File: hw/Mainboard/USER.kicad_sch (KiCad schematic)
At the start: 4 parts, among them J13 USER, J14 USER_HEADER

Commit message: hw: 2x config switch (wip)
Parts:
- renumbered J13 to J12, J14 to J13
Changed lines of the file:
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@@
   (symbol (lib_id "Retrocomputing:CBM_PET_USER_Conn_02x12_Card_Edge") (at 106.68 93.98 0) (unit 1)
     (in_bom yes) (on_board yes)
-    (property "Reference" "J13" (id 0) (at 107.95 75.7682 0))
+    (property "Reference" "J12" (id 0) (at 107.95 75.7682 0))
     (property "Value" "USER" (id 1) (at 107.95 78.0796 0))
     (property "Footprint" "Retrocomputing:CBM_PET_USER_EDGE_CON_24P" (id 2) (at 106.68 93.98 0)
@@
   (symbol (lib_id "Connector_Generic:Conn_02x11_Odd_Even") (at 176.53 95.25 0) (mirror x) (unit 1)
     (in_bom yes) (on_board yes) (fields_autoplaced)
-    (property "Reference" "J14" (id 0) (at 177.8 76.2 0))
+    (property "Reference" "J13" (id 0) (at 177.8 76.2 0))
     (property "Value" "USER_HEADER" (id 1) (at 177.8 78.74 0))
     (property "Footprint" "Connector_PinHeader_2.54mm:PinHeader_2x11_P2.54mm_Vertical" (id 2) (at 176.53 95.25 0)
@@
   (symbol (lib_id "PET:PD_GND") (at 107.95 111.76 0) (unit 1)
     (in_bom yes) (on_board yes) (fields_autoplaced)
-    (property "Reference" "#PWR0107" (id 0) (at 107.95 118.11 0)
+    (property "Reference" "#PWR0113" (id 0) (at 107.95 118.11 0)
       (effects (font (size 1.27 1.27)) hide)
     )
@@
   (symbol (lib_id "PET:PD_GND") (at 133.35 82.55 0) (unit 1)
     (in_bom yes) (on_board yes) (fields_autoplaced)
-    (property "Reference" "#PWR0105" (id 0) (at 133.35 88.9 0)
+    (property "Reference" "#PWR0111" (id 0) (at 133.35 88.9 0)
       (effects (font (size 1.27 1.27)) hide)
     )
@@
   (symbol (lib_id "PET:PD_GND") (at 171.45 109.22 0) (unit 1)
     (in_bom yes) (on_board yes) (fields_autoplaced)
-    (property "Reference" "#PWR0106" (id 0) (at 171.45 115.57 0)
+    (property "Reference" "#PWR0112" (id 0) (at 171.45 115.57 0)
       (effects (font (size 1.27 1.27)) hide)
     )
@@
   (symbol (lib_id "power:+5V") (at 85.09 78.74 0) (mirror y) (unit 1)
     (in_bom yes) (on_board yes)
-    (property "Reference" "#PWR0104" (id 0) (at 85.09 82.55 0)
+    (property "Reference" "#PWR0110" (id 0) (at 85.09 82.55 0)
       (effects (font (size 1.27 1.27)) hide)
     )

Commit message: hw: header_and_jumper, button for flashing (wip)
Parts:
- JP1: footprint Jumper:SolderJumper-3_P1.3mm_Open_RoundedPad1.0x1.5mm -> PET:PinHeader_and_Jumper_1x03_P2.54mm_Vertical
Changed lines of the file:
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@@
     (property "Reference" "JP1" (id 0) (at 69.85 73.66 0))
     (property "Value" "VIDEO_OR_5V" (id 1) (at 69.85 76.2 0))
-    (property "Footprint" "Jumper:SolderJumper-3_P1.3mm_Open_RoundedPad1.0x1.5mm" (id 2) (at 69.85 78.74 0)
+    (property "Footprint" "PET:PinHeader_and_Jumper_1x03_P2.54mm_Vertical" (id 2) (at 69.85 78.74 0)
       (effects (font (size 1.27 1.27)) hide)
     )

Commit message: hw: caps & logos (wip)
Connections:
- net VCC is gone; now on net +5V: J13.2 (Pin_2), JP1.3 (B), PT37.2
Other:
- title: CBM PET Mainboard Replacement -> EconoPET 40/8096
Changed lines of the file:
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@@
   (paper "A")
   (title_block
-    (title "CBM PET Mainboard Replacement")
+    (title "EconoPET 40/8096")
+    (date "2023-10-01")
+    (rev "A")
+  )
+  (junction (at 83.82 78.74) (diameter 0) (color 0 0 0 0)
+  )
+  (junction (at 78.74 78.74) (diameter 0) (color 0 0 0 0)
   )
   (junction (at 107.95 111.76) (diameter 0) (color 0 0 0 0)
@@
     (stroke (width 0) (type default) (color 0 0 0 0))
   )
+  (wire (pts (xy 78.74 78.74) (xy 83.82 78.74))
+    (stroke (width 0) (type default) (color 0 0 0 0))
+  )

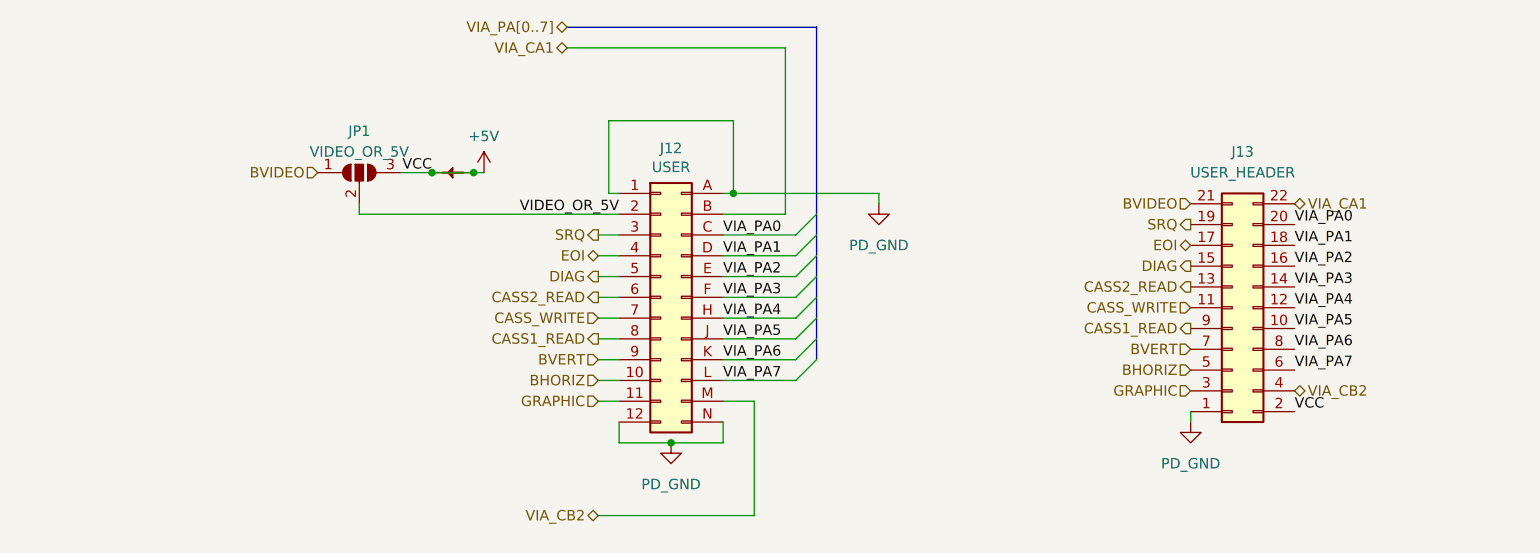
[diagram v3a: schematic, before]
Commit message: hw: remove net/power ties
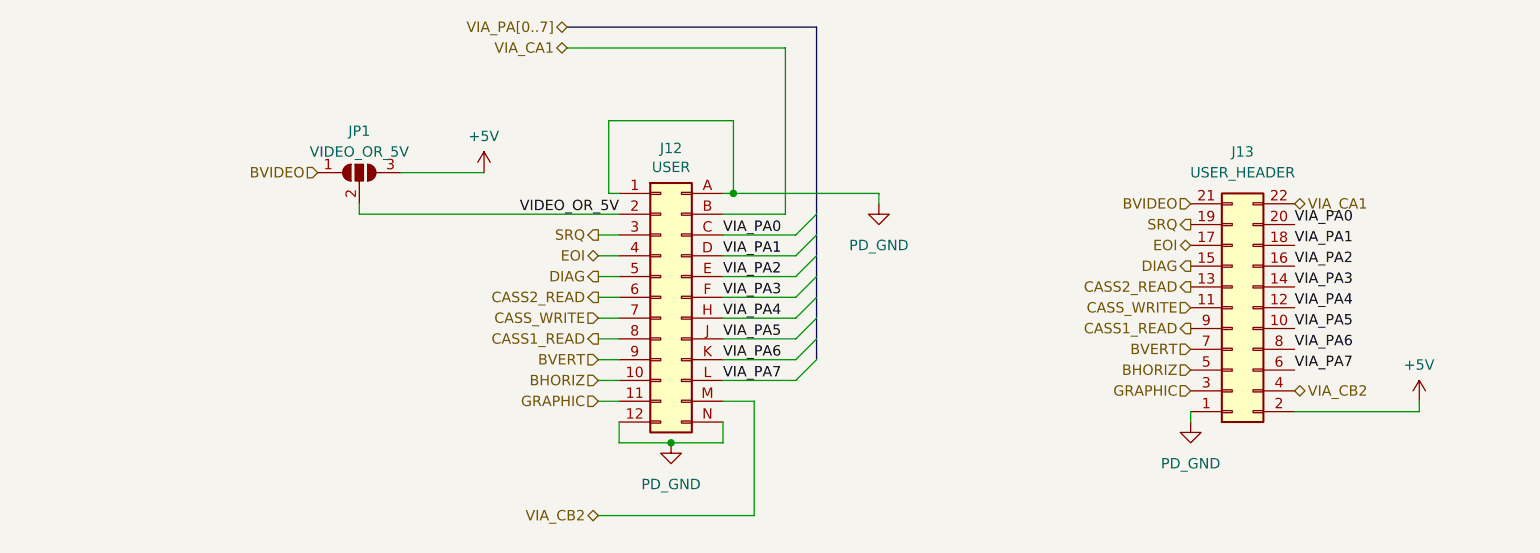
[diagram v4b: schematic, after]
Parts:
- removed PT37: PowerTie_2, PET:NetTie-2_SMD_Pad_1.6_to_0.4mm, symbol PET:PowerTie_2
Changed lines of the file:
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@@
     (rev "A")
   )
-  (junction (at 83.82 78.74) (diameter 0) (color 0 0 0 0)
-  )
-  (junction (at 78.74 78.74) (diameter 0) (color 0 0 0 0)
-  )
   (junction (at 107.95 111.76) (diameter 0) (color 0 0 0 0)
   )
@@
     (stroke (width 0) (type default) (color 0 0 0 0))
   )
+  (wire (pts (xy 184.15 107.95) (xy 199.39 107.95))
+    (stroke (width 0) (type default) (color 0 0 0 0))
+  )
   (wire (pts (xy 69.85 83.82) (xy 69.85 82.55))
     (stroke (width 0) (type default) (color 0 0 0 0))
@@
     (stroke (width 0) (type default) (color 0 0 0 0))
   )
+  (wire (pts (xy 199.39 107.95) (xy 199.39 106.68))
+    (stroke (width 0) (type default) (color 0 0 0 0))
+  )
   (bus (pts (xy 125.73 60.96) (xy 95.25 60.96))
     (stroke (width 0) (type default) (color 0 0 0 0))
   )
-  (wire (pts (xy 78.74 78.74) (xy 74.93 78.74))
+  (wire (pts (xy 74.93 78.74) (xy 85.09 78.74))
     (stroke (width 0) (type default) (color 0 0 0 0))
   )
@@
     (stroke (width 0) (type default) (color 0 0 0 0))
   )
-  (wire (pts (xy 83.82 78.74) (xy 85.09 78.74))
-    (stroke (width 0) (type default) (color 0 0 0 0))
-  )
   (wire (pts (xy 99.06 86.36) (xy 101.6 86.36))
     (stroke (width 0) (type default) (color 0 0 0 0))
   )
-  (wire (pts (xy 78.74 78.74) (xy 83.82 78.74))
-    (stroke (width 0) (type default) (color 0 0 0 0))
-  )
   (bus (pts (xy 125.73 99.06) (xy 125.73 101.6))
     (stroke (width 0) (type default) (color 0 0 0 0))
@@
   )
   (label "VIA_PA5" (at 184.15 97.79 0)
-    (effects (font (size 1.27 1.27)) (justify left bottom))
-  )
-  (label "VCC" (at 184.15 107.95 0)
     (effects (font (size 1.27 1.27)) (justify left bottom))
   )
@@
   (label "VIA_PA0" (at 114.3 86.36 0)
     (effects (font (size 1.27 1.27)) (justify left bottom))
-  )
-  (label "VCC" (at 78.74 78.74 180)
-    (effects (font (size 1.27 1.27)) (justify right bottom))
   )
   (label "VIA_PA3" (at 184.15 92.71 0)
@@
     (pin "N")
   )
+  (symbol (lib_id "power:+5V") (at 199.39 106.68 0) (mirror y) (unit 1)
+    (in_bom yes) (on_board yes)
+    (property "Reference" "#PWR0191" (id 0) (at 199.39 110.49 0)
+      (effects (font (size 1.27 1.27)) hide)
+    )
+    (property "Value" "+5V" (id 1) (at 197.485 102.235 0)
+      (effects (font (size 1.27 1.27)) (justify right))
+    )
+    (property "Footprint" "" (id 2) (at 199.39 106.68 0)
+      (effects (font (size 1.27 1.27)) hide)
+    )
+    (property "Datasheet" "" (id 3) (at 199.39 106.68 0)
+      (effects (font (size 1.27 1.27)) hide)
+    )
+    (pin "1")
+  )
   (symbol (lib_id "Connector_Generic:Conn_02x11_Odd_Even") (at 176.53 95.25 0) (mirror x) (unit 1)
     (in_bom yes) (on_board yes) (fields_autoplaced)
@@
     (pin "9")
   )
-  (symbol (lib_id "PET:PowerTie_2") (at 81.28 78.74 180) (unit 1)
-    (in_bom yes) (on_board yes) (fields_autoplaced)
-    (property "Reference" "PT37" (id 0) (at 81.28 80.645 0)
-      (effects (font (size 1.27 1.27)) hide)
-    )
-    (property "Value" "PowerTie_2" (id 1) (at 81.28 76.835 0)
-      (effects (font (size 1.27 1.27)) hide)
-    )
-    (property "Footprint" "PET:NetTie-2_SMD_Pad_1.6_to_0.4mm" (id 2) (at 81.28 78.74 0)
-      (effects (font (size 1.27 1.27)) hide)
-    )
-    (property "Datasheet" "~" (id 3) (at 81.28 78.74 0)
-      (effects (font (size 1.27 1.27)) hide)
-    )
-    (pin "1")
-    (pin "2")
-  )
   (symbol (lib_id "PET:PD_GND") (at 107.95 111.76 0) (unit 1)

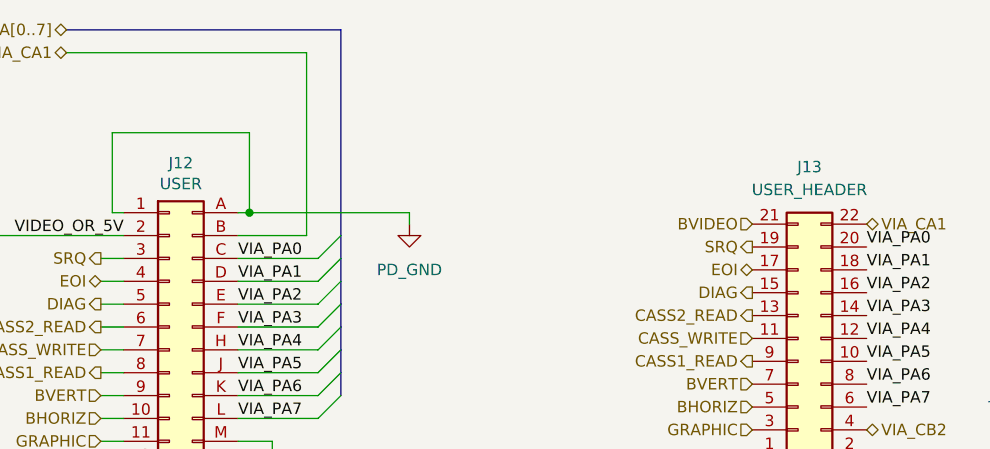
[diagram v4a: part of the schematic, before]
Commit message: hw: renumber J* refs to match PET connectors
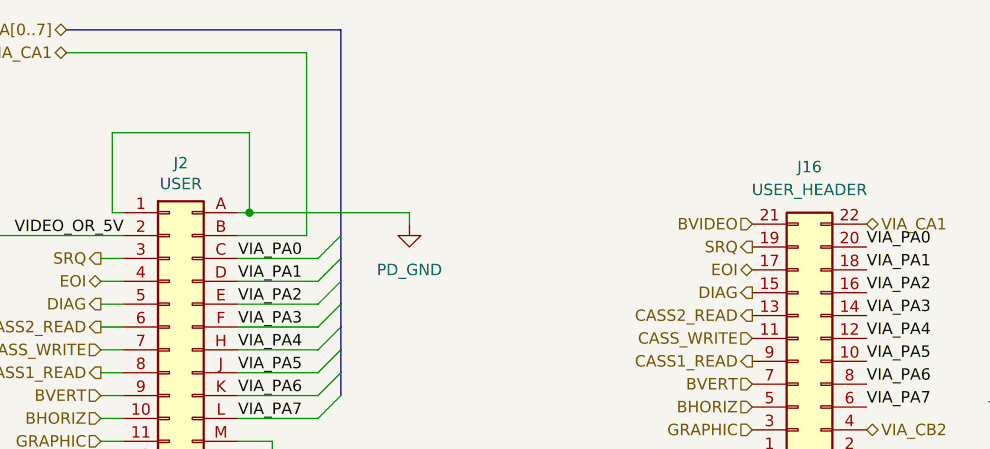
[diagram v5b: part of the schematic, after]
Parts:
- renumbered J13 to J16, J12 to J2
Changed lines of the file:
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@@
   (symbol (lib_id "Retrocomputing:CBM_PET_USER_Conn_02x12_Card_Edge") (at 106.68 93.98 0) (unit 1)
     (in_bom yes) (on_board yes)
-    (property "Reference" "J12" (id 0) (at 107.95 75.7682 0))
+    (property "Reference" "J2" (id 0) (at 107.95 75.7682 0))
     (property "Value" "USER" (id 1) (at 107.95 78.0796 0))
     (property "Footprint" "Retrocomputing:CBM_PET_USER_EDGE_CON_24P" (id 2) (at 106.68 93.98 0)
@@
   (symbol (lib_id "power:+5V") (at 199.39 106.68 0) (mirror y) (unit 1)
     (in_bom yes) (on_board yes)
-    (property "Reference" "#PWR0191" (id 0) (at 199.39 110.49 0)
+    (property "Reference" "#PWR0121" (id 0) (at 199.39 110.49 0)
       (effects (font (size 1.27 1.27)) hide)
     )
@@
   (symbol (lib_id "Connector_Generic:Conn_02x11_Odd_Even") (at 176.53 95.25 0) (mirror x) (unit 1)
     (in_bom yes) (on_board yes) (fields_autoplaced)
-    (property "Reference" "J13" (id 0) (at 177.8 76.2 0))
+    (property "Reference" "J16" (id 0) (at 177.8 76.2 0))
     (property "Value" "USER_HEADER" (id 1) (at 177.8 78.74 0))
     (property "Footprint" "Connector_PinHeader_2.54mm:PinHeader_2x11_P2.54mm_Vertical" (id 2) (at 176.53 95.25 0)
@@
   (symbol (lib_id "PET:PD_GND") (at 107.95 111.76 0) (unit 1)
     (in_bom yes) (on_board yes) (fields_autoplaced)
-    (property "Reference" "#PWR0113" (id 0) (at 107.95 118.11 0)
+    (property "Reference" "#PWR0118" (id 0) (at 107.95 118.11 0)
       (effects (font (size 1.27 1.27)) hide)
     )
@@
   (symbol (lib_id "PET:PD_GND") (at 133.35 82.55 0) (unit 1)
     (in_bom yes) (on_board yes) (fields_autoplaced)
-    (property "Reference" "#PWR0111" (id 0) (at 133.35 88.9 0)
+    (property "Reference" "#PWR0119" (id 0) (at 133.35 88.9 0)
       (effects (font (size 1.27 1.27)) hide)
     )
@@
   (symbol (lib_id "PET:PD_GND") (at 171.45 109.22 0) (unit 1)
     (in_bom yes) (on_board yes) (fields_autoplaced)
-    (property "Reference" "#PWR0112" (id 0) (at 171.45 115.57 0)
+    (property "Reference" "#PWR0120" (id 0) (at 171.45 115.57 0)
       (effects (font (size 1.27 1.27)) hide)
     )
@@
   (symbol (lib_id "power:+5V") (at 85.09 78.74 0) (mirror y) (unit 1)
     (in_bom yes) (on_board yes)
-    (property "Reference" "#PWR0110" (id 0) (at 85.09 82.55 0)
+    (property "Reference" "#PWR0117" (id 0) (at 85.09 82.55 0)
       (effects (font (size 1.27 1.27)) hide)
     )

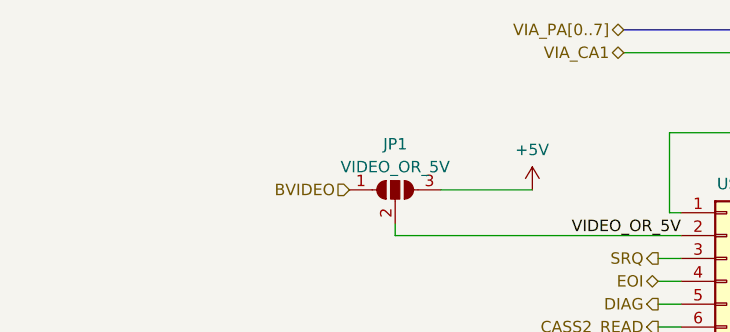
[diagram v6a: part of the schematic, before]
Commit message: hw: comments in schematics
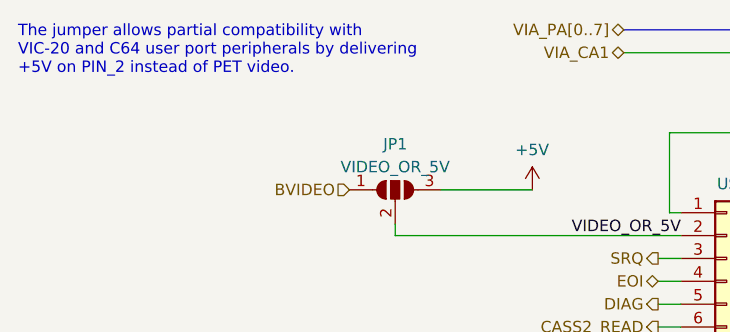
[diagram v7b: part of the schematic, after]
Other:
- note added: "The jumper allows partial compatibility with VIC-20 and C64 user port peripherals by delivering +5V on PIN_2 instead of PET video."
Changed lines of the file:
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@@
     (stroke (width 0) (type default) (color 0 0 0 0))
+  )
+  (text "The jumper allows partial compatibility with\nVIC-20 and C64 user port peripherals by delivering\n+5V on PIN_2 instead of PET video."
+    (at 27.94 66.04 0)
+    (effects (font (size 1.27 1.27)) (justify left bottom))
   )
   (label "VIA_PA0" (at 184.15 85.09 0)

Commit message: hw: tidy
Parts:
- added C104: 4.7u 10V, Capacitor_SMD:C_0402_1005Metric, symbol Device:C_Small
- JP1: footprint PET:PinHeader_and_Jumper_1x03_P2.54mm_Vertical -> Jumper:SolderJumper-3_P1.3mm_Open_RoundedPad1.0x1.5mm
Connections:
- net +5V: now also C104.1
- net PD_GND: now also C104.2
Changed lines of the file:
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@@
     (rev "A")
   )
+  (junction (at 199.39 107.95) (diameter 0) (color 0 0 0 0)
+  )
   (junction (at 107.95 111.76) (diameter 0) (color 0 0 0 0)
   )
+  (junction (at 185.42 115.57) (diameter 0) (color 0 0 0 0)
+  )
   (junction (at 115.57 81.28) (diameter 0) (color 0 0 0 0)
   )
@@
     (stroke (width 0) (type default) (color 0 0 0 0))
   )
+  (wire (pts (xy 199.39 114.3) (xy 199.39 115.57))
+    (stroke (width 0) (type default) (color 0 0 0 0))
+  )
   (wire (pts (xy 184.15 107.95) (xy 199.39 107.95))
     (stroke (width 0) (type default) (color 0 0 0 0))
@@
     (stroke (width 0) (type default) (color 0 0 0 0))
   )
-  (wire (pts (xy 171.45 109.22) (xy 171.45 107.95))
+  (wire (pts (xy 171.45 107.95) (xy 171.45 115.57))
     (stroke (width 0) (type default) (color 0 0 0 0))
   )
@@
     (stroke (width 0) (type default) (color 0 0 0 0))
   )
+  (wire (pts (xy 185.42 115.57) (xy 171.45 115.57))
+    (stroke (width 0) (type default) (color 0 0 0 0))
+  )
   (wire (pts (xy 199.39 107.95) (xy 199.39 106.68))
     (stroke (width 0) (type default) (color 0 0 0 0))
@@
     (stroke (width 0) (type default) (color 0 0 0 0))
   )
+  (wire (pts (xy 199.39 107.95) (xy 199.39 109.22))
+    (stroke (width 0) (type default) (color 0 0 0 0))
+  )
   (wire (pts (xy 114.3 109.22) (xy 114.3 111.76))
     (stroke (width 0) (type default) (color 0 0 0 0))
@@
     (stroke (width 0) (type default) (color 0 0 0 0))
   )
+  (wire (pts (xy 185.42 116.84) (xy 185.42 115.57))
+    (stroke (width 0) (type default) (color 0 0 0 0))
+  )
   (wire (pts (xy 114.3 101.6) (xy 123.19 101.6))
     (stroke (width 0) (type default) (color 0 0 0 0))
@@
     (stroke (width 0) (type default) (color 0 0 0 0))
   )
+  (wire (pts (xy 185.42 115.57) (xy 199.39 115.57))
+    (stroke (width 0) (type default) (color 0 0 0 0))
+  )
   (wire (pts (xy 114.3 106.68) (xy 118.11 106.68))
     (stroke (width 0) (type default) (color 0 0 0 0))
@@
     (stroke (width 0) (type default) (color 0 0 0 0))
   )
-  (text "The jumper allows partial compatibility with\nVIC-20 and C64 user port peripherals by delivering\n+5V on PIN_2 instead of PET video."
+  (text "The jumper allows partial compatibility with\nVIC-20 and C64 user port peripherals by\ndelivering +5V on PIN_2 instead of PET video."
     (at 27.94 66.04 0)
     (effects (font (size 1.27 1.27)) (justify left bottom))
@@
     (pin "1")
   )
+  (symbol (lib_id "Device:C_Small") (at 199.39 111.76 0) (unit 1)
+    (in_bom yes) (on_board yes)
+    (property "Reference" "C104" (id 0) (at 201.7268 110.5916 0)
+      (effects (font (size 1.27 1.27)) (justify left))
+    )
+    (property "Value" "4.7u 10V" (id 1) (at 201.7268 112.903 0)
+      (effects (font (size 1.27 1.27)) (justify left))
+    )
+    (property "Footprint" "Capacitor_SMD:C_0402_1005Metric" (id 2) (at 199.39 111.76 0)
+      (effects (font (size 1.27 1.27)) hide)
+    )
+    (property "Datasheet" "https://datasheet.lcsc.com/lcsc/2304140030_Samsung-Electro-Mechanics-CL05A475MP5NRNC_C23733.pdf" (id 3) (at 199.39 111.76 0)
+      (effects (font (size 1.27 1.27)) hide)
+    )
+    (property "LCSC" "C23733" (id 4) (at 199.39 111.76 0)
+      (effects (font (size 1.27 1.27)) hide)
+    )
+    (pin "1")
+    (pin "2")
+  )
   (symbol (lib_id "PET:PD_GND") (at 133.35 82.55 0) (unit 1)
     (in_bom yes) (on_board yes) (fields_autoplaced)
@@
     (property "Reference" "JP1" (id 0) (at 69.85 73.66 0))
     (property "Value" "VIDEO_OR_5V" (id 1) (at 69.85 76.2 0))
-    (property "Footprint" "PET:PinHeader_and_Jumper_1x03_P2.54mm_Vertical" (id 2) (at 69.85 78.74 0)
+    (property "Footprint" "Jumper:SolderJumper-3_P1.3mm_Open_RoundedPad1.0x1.5mm" (id 2) (at 69.85 78.74 0)
       (effects (font (size 1.27 1.27)) hide)
     )
@@
     (pin "3")
   )
-  (symbol (lib_id "PET:PD_GND") (at 171.45 109.22 0) (unit 1)
+  (symbol (lib_id "PET:PD_GND") (at 185.42 116.84 0) (unit 1)
     (in_bom yes) (on_board yes) (fields_autoplaced)
-    (property "Reference" "#PWR0120" (id 0) (at 171.45 115.57 0)
-      (effects (font (size 1.27 1.27)) hide)
-    )
-    (property "Value" "PD_GND" (id 1) (at 171.45 114.3 0))
-    (property "Footprint" "" (id 2) (at 171.45 109.22 0)
-      (effects (font (size 1.27 1.27)) hide)
-    )
-    (property "Datasheet" "" (id 3) (at 171.45 109.22 0)
-      (effects (font (size 1.27 1.27)) hide)
-    )
+    (property "Reference" "#PWR0120" (id 0) (at 185.42 123.19 0)
+      (effects (font (size 1.27 1.27)) hide)
+    )
+    (property "Value" "PD_GND" (id 1) (at 185.42 121.92 0))
+    (property "Footprint" "" (id 2) (at 185.42 116.84 0)
+      (effects (font (size 1.27 1.27)) hide)
+    )
+    (property "Datasheet" "" (id 3) (at 185.42 116.84 0)
+      (effects (font (size 1.27 1.27)) hide)
+    )
